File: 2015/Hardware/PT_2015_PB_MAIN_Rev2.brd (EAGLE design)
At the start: 142.2 x 170.8 mm, 137 parts, among them Q1 Q_ACS711LC, Q11 Q_IRFS7437PbF, Q12 2N7002, Q14 Q_IRFS7437PbF, Q16 Q_IRFS7437PbF, Q18 Q_FDT86102LZ, Q20 Q_IRFS7437PbF, Q4 Q_ACS711LC, Q5 Q_ACS711LC, Q6 Q_IRFS7437PbF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

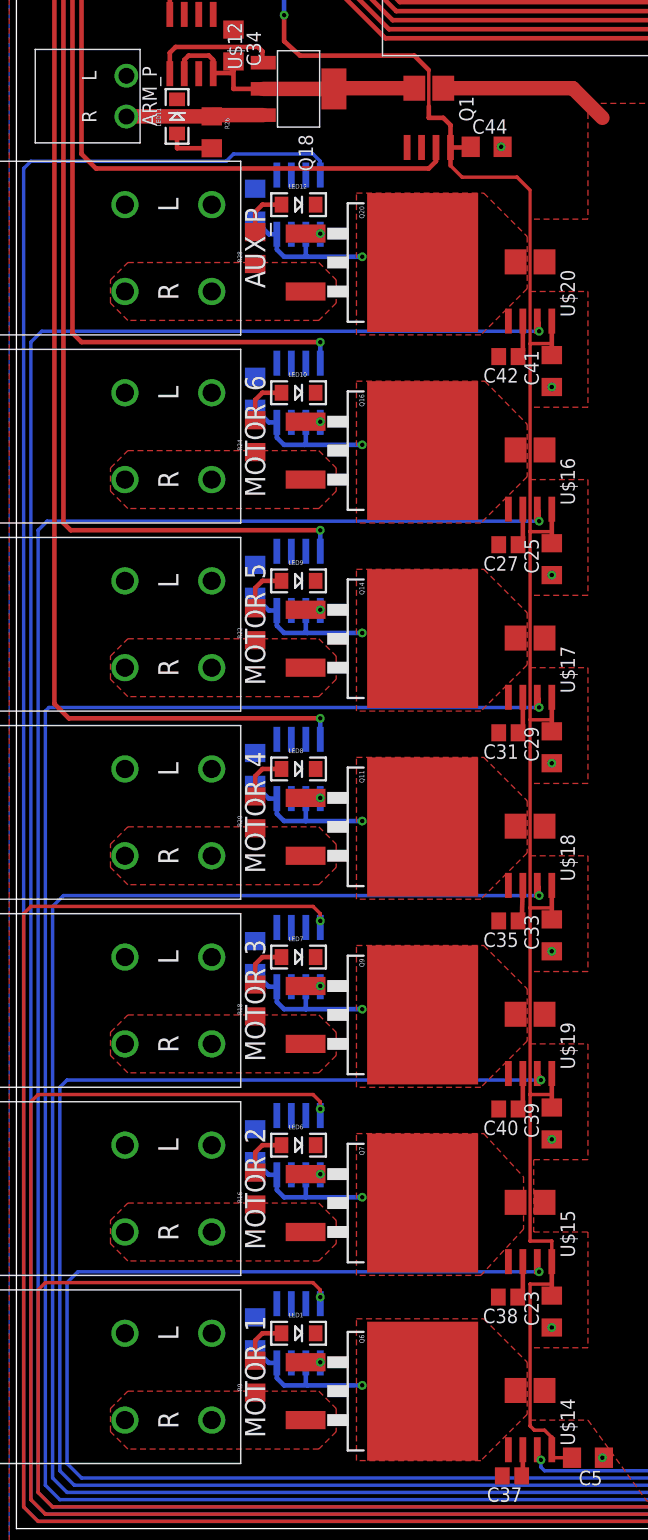
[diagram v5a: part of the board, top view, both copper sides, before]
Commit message: Fixed DRC Errors for 3oz Copper
Brought board to spec for 4PCB's 3oz Copper
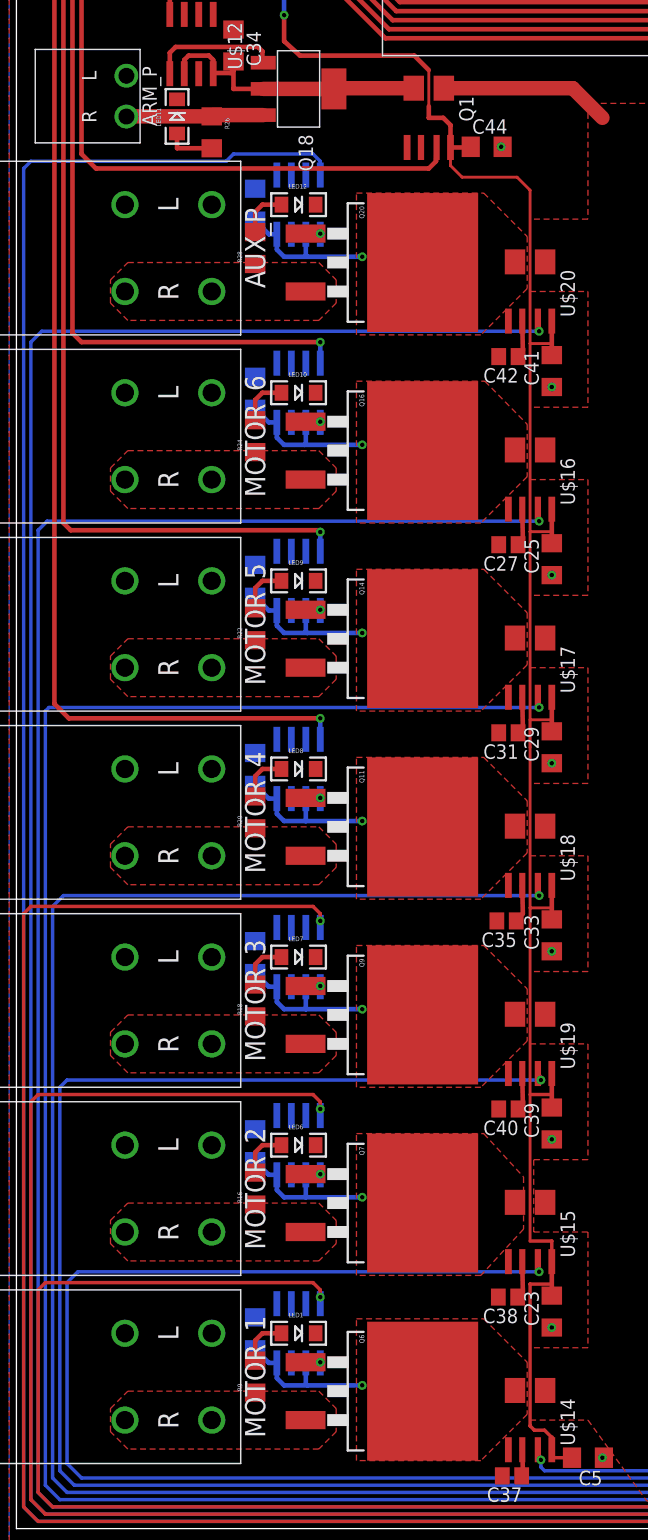
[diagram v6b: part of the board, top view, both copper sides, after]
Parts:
- Q1: value Q_ACS711LC -> Q_ACS711LC_SKETCH; device MRDT-2015-PowerBoard:SOIC8_ACS711 -> MRDT-2015-PowerBoard:SOIC8_ACS711_SKETCH
- U$14, U$15, U$16, U$17, U$18, U$19, U$20: device MRDT-2015-PowerBoard:SOIC8_ACS711 -> MRDT-2015-PowerBoard:SOIC8_ACS711_SKETCH
- moved C35 0.16 mm to (38.6, 48.9)

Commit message: Added LEDs, a buzzer, and adjusted traces
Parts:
- added LED13, LED14: (no value), SparkFun-LED:FKIT-LED-1206
- added R1, R2: 1k Ohm, SparkFun-Passives:1206
- added SG1: BUZZERSMD2, SparkFun-Electromechanical:BUZZER-CCV
- moved LED4 3.18 mm to (128.9, 134.6)
- moved C12 1.91 mm to (128.9, 122.4), turned to 270 degrees
- moved R12 1.91 mm to (128.9, 128.4), turned to 90 degrees
- moved R7 0.06 mm to (100.3, 57.6), flipped to the bottom, turned to 180 degrees
- flipped R8 to the bottom, turned to 180 degrees
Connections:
- new net BUZZ_BUZZ_MOTHERFUCKER: SG1.-, U$1.8
- new net INFO_LED_1: R1.1, U$1.9
- new net INFO_LED_2: R2.1, U$1.10
- new net N$11: LED13.A, R1.2
- new net N$32: LED14.A, R2.2
- net AUX_P-IMEAS: now also U$1.30; no longer U$1.27
- net AUX_P-SIG: now also U$1.11; no longer U$1.8
- net GND: now also LED13.C, LED14.C, SG1.+
- net M1-SIG: now also U$1.25; no longer U$1.28
- net M2-SIG: now also U$1.26; no longer U$1.29
- net M3-SIG: now also U$1.27; no longer U$1.30
- net M5-IMEAS: now also U$1.28; no longer U$1.25
- net M6-IMEAS: now also U$1.29; no longer U$1.26
- net N$5: now also L6.9
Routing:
- net BUZZ_BUZZ_MOTHERFUCKER: track 0.00 -> 42.7 mm
- net N$32: track 0.00 -> 15.6 mm
- net N$11: track 0.00 -> 10.1 mm
- net INFO_LED_1: track 0.00 -> 8.16 mm
- net AUX_P-SIG: track 327.2 -> 334.9 mm
- net M5-IMEAS: track 259.4 -> 255.1 mm
- net AUX_P-IMEAS: track 294.7 -> 297.8 mm
- net M1-SIG: track 188.7 -> 191.3 mm
- net INFO_LED_2: track 0.00 -> 2.60 mm
- net N$50: track 5.30 -> 3.37 mm
- net M6-IMEAS: track 278.0 -> 276.2 mm
- net M2-SIG: track 209.2 -> 210.2 mm
- net M3-SIG: track 229.7 -> 229.1 mm
- net 12V-SIG: vias 1 -> 0

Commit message: Fixed some values
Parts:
- C10, C15: value (none) -> 2.2µF
- C8: value 47µf -> 10µf
- R3: value 70kΩ -> 60kΩ
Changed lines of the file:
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@@
 <?xml version="1.0" encoding="utf-8"?>
 <!DOCTYPE eagle SYSTEM "eagle.dtd">
-<eagle version="6.5.0">
+<eagle version="7.0.0">
 <drawing>
 <settings>
@@
 <pass name="Default">
 <param name="RoutingGrid" value="50mil"/>
+<param name="AutoGrid" value="1"/>
+<param name="Efforts" value="0"/>
+<param name="TopRouterVariant" value="1"/>
 <param name="tpViaShape" value="round"/>
 <param name="PrefDir.1" value="|"/>
@@
 <element name="R5" library="SparkFun-Passives" package="1206" value="120 Ohm" x="118.491" y="41.91" rot="R270"/>
 <element name="R6" library="SparkFun-Passives" package="1206" value="120 Ohm" x="118.491" y="36.83" rot="R270"/>
-<element name="R3" library="resistor" package="R1206" value="70kΩ" x="80.645" y="32.258" rot="R180"/>
+<element name="R3" library="resistor" package="R1206" value="60kΩ" x="80.645" y="32.258" rot="R180"/>
 <element name="R4" library="resistor" package="R1206" value="10kΩ" x="86.36" y="32.258" rot="R180"/>
 <element name="C11" library="resistor" package="C1206" value="" x="132.715" y="93.98"/>
 <element name="C12" library="resistor" package="C1206" value="47µf" x="128.905" y="122.39625" rot="R270"/>
 <element name="C13" library="resistor" package="C1206" value="2.2µF" x="81.28" y="95.25" rot="R270"/>
-<element name="C15" library="resistor" package="C1206" value="" x="80.01" y="78.74" rot="R180"/>
+<element name="C15" library="resistor" package="C1206" value="2.2µF" x="80.01" y="78.74" rot="R180"/>
 <element name="R8" library="resistor" package="R1206" value="21kΩ" x="100.33" y="83.185" rot="MR180"/>
 <element name="Q4" library="MRDT-2015-PowerBoard" package="SOIC8_ACS711" value="Q_ACS711LC" x="130.81" y="115.57" rot="R90"/>
@@
 <element name="R7" library="resistor" package="R1206" value="590Ω" x="100.33" y="57.5945" rot="MR180"/>
 <element name="C7" library="resistor" package="C1206" value="1uF" x="107.696" y="39.37" rot="R270"/>
-<element name="C8" library="resistor" package="C1206" value="47µf" x="132.715" y="62.865"/>
+<element name="C8" library="resistor" package="C1206" value="10µf" x="132.715" y="62.865"/>
 <element name="U$5" library="MRDT-2014-All" package="SOD-323" value="D_SD12T1G" x="127" y="77.47" rot="R180"/>
 <element name="C9" library="resistor" package="C1206" value="" x="126.365" y="74.93" rot="R180"/>
-<element name="C10" library="resistor" package="C1206" value="" x="81.153" y="52.197" rot="R180"/>
+<element name="C10" library="resistor" package="C1206" value="2.2µF" x="81.153" y="52.197" rot="R180"/>
 <element name="C14" library="resistor" package="C1206" value="2.2µF" x="81.28" y="68.58" rot="R270"/>
 <element name="BATT-POS" library="MRDT-2015-PowerBoard" package="LARGE_TERMINAL_HOLE" value="TERMINAL_HOLE" x="63.5" y="12.7"/>
